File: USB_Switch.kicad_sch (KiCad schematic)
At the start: 1 part

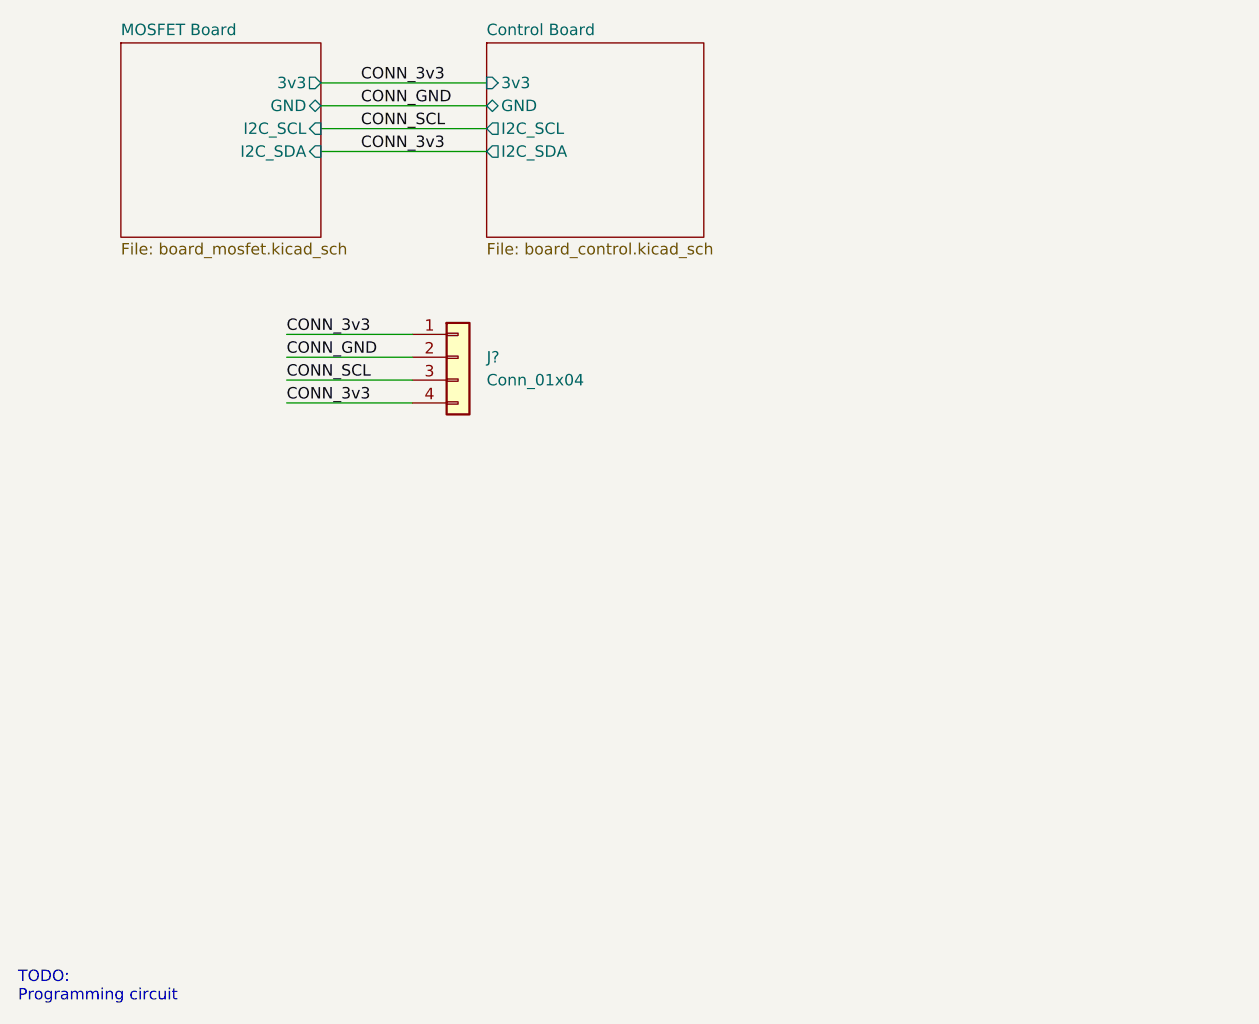
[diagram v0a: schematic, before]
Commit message: Fixed file name, started board layout
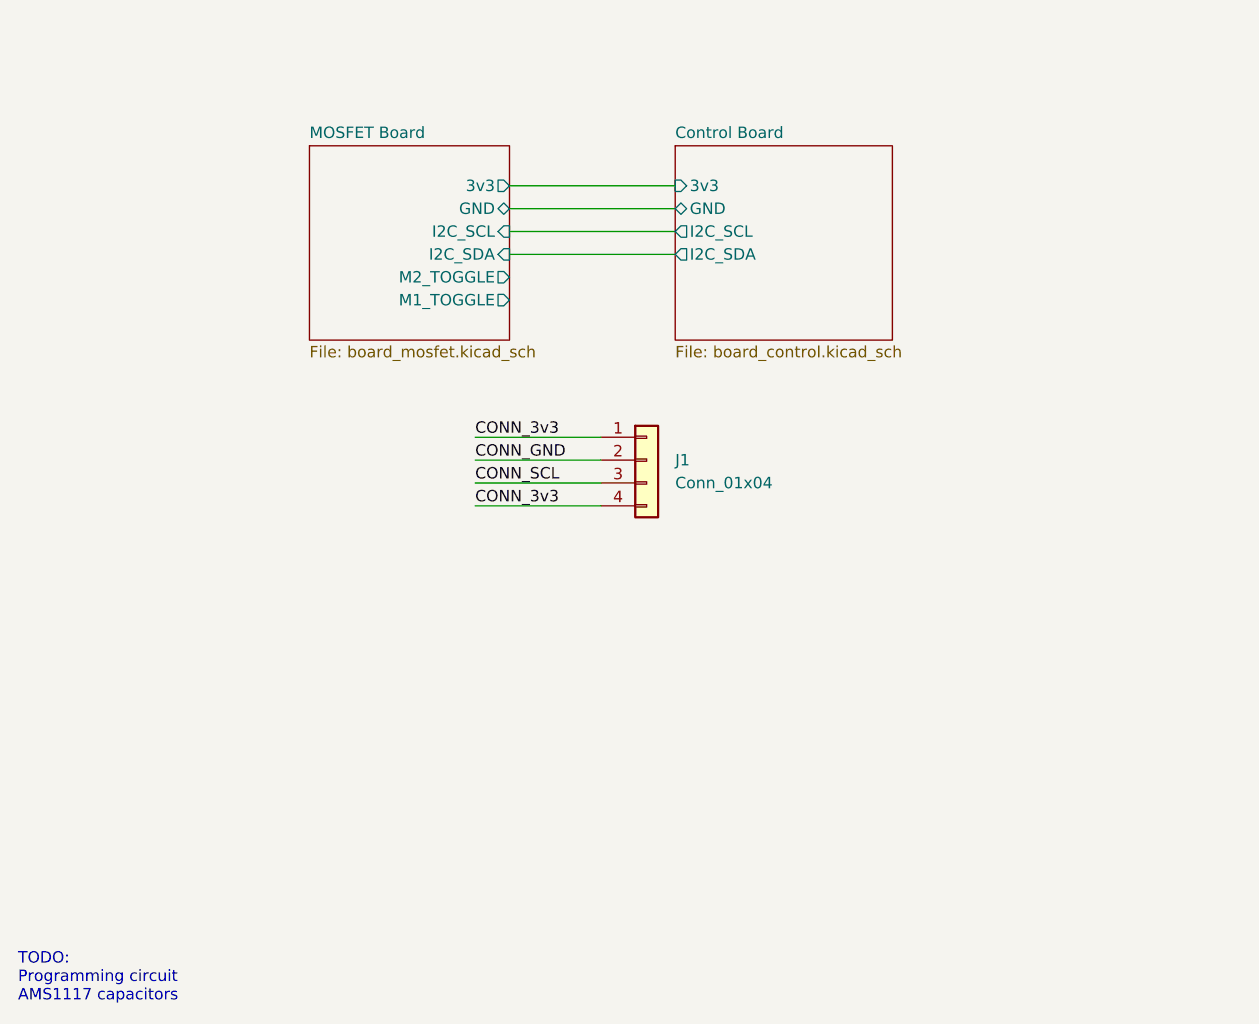
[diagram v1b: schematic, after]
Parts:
- gave numbers to parts that had none: 1
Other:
- sheet MOSFET Board ports: added M1_TOGGLE, M2_TOGGLE; removed none
- note added: "TODO: Programming circuit AMS1117 capacitors"
- note removed: "TODO: Programming circuit"
- moved on the sheet: J1

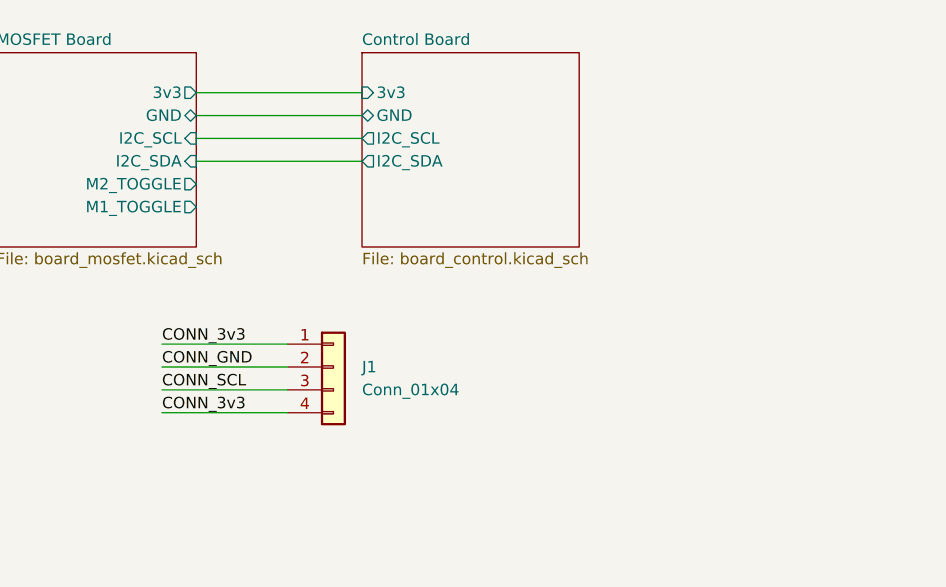
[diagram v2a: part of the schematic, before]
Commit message: Updated board connections. Added supplier info for all parts
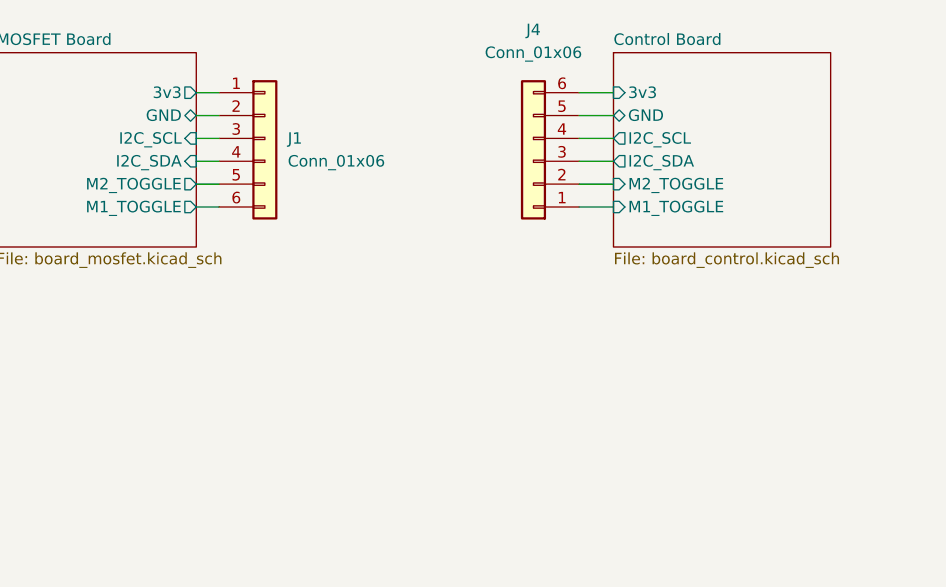
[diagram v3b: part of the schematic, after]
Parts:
- removed J1: Conn_01x04, symbol Connector_Generic:Conn_01x04
- added J1, J4: Conn_01x06, Connector_PinHeader_2.54mm:PinHeader_1x06_P2.54mm_Vertical, symbol Connector_Generic:Conn_01x06
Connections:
- net Control Board/3v3: now also J4.6 (Pin_6)
- net Control Board/GND: now also J4.5 (Pin_5)
- net Control Board/I2C_SCL: now also J4.4 (Pin_4)
- net Control Board/I2C_SDA: now also J4.3 (Pin_3)
- net MOSFET Board/M1_TOGGLE: now also J1.6 (Pin_6)
- net MOSFET Board/M2_TOGGLE: now also J1.5 (Pin_5)
- new net Control Board/M1_TOGGLE: J4.1 (Pin_1)
- new net Control Board/M2_TOGGLE: J4.2 (Pin_2)
- new net MOSFET Board/3v3: J1.1 (Pin_1)
- new net MOSFET Board/GND: J1.2 (Pin_2)
- new net MOSFET Board/I2C_SCL: J1.3 (Pin_3)
- new net MOSFET Board/I2C_SDA: J1.4 (Pin_4)
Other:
- sheet Control Board ports: added M1_TOGGLE, M2_TOGGLE; removed none

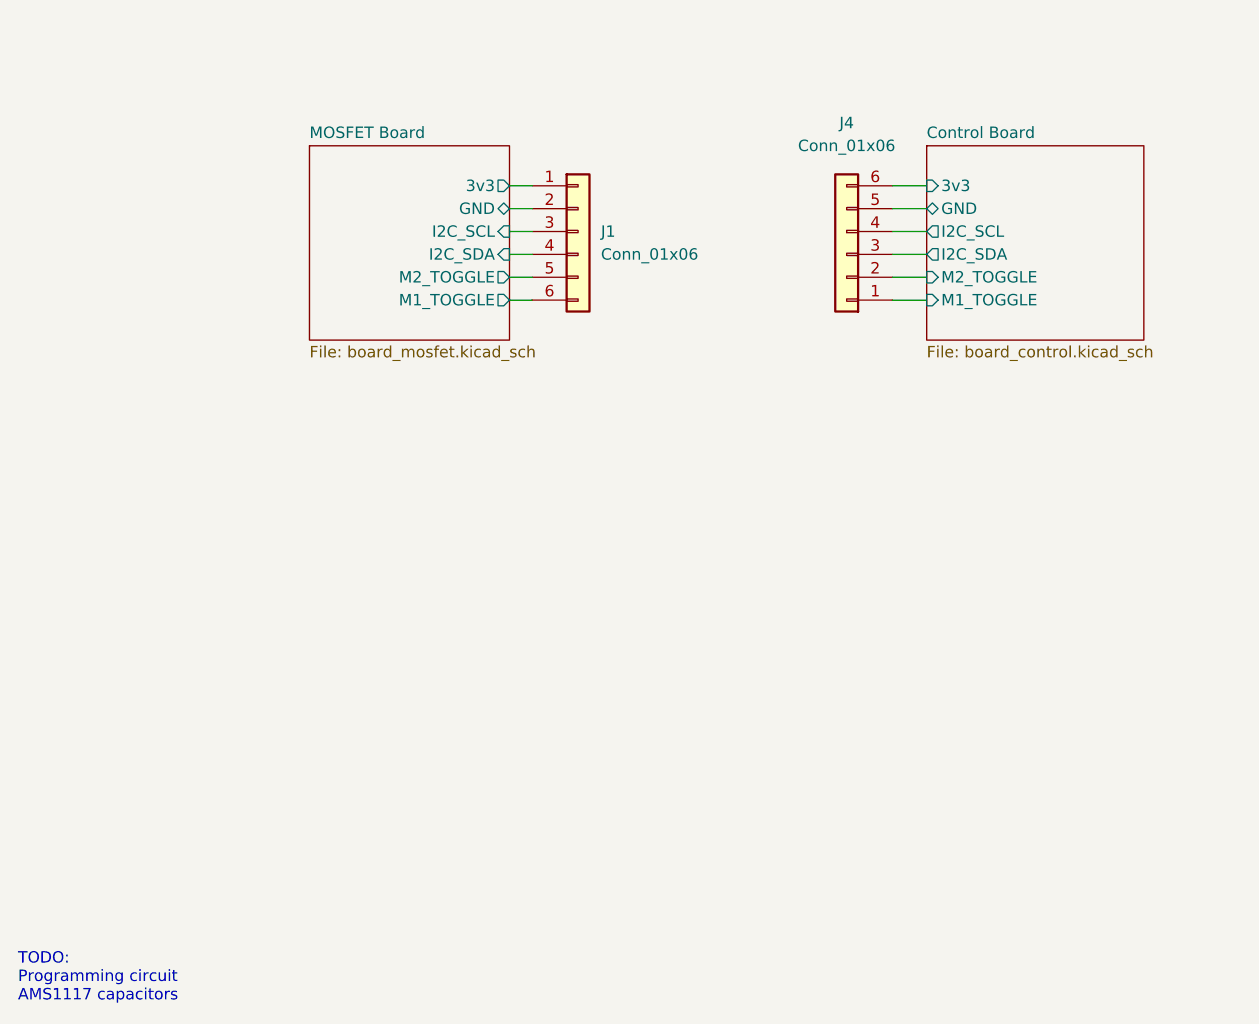
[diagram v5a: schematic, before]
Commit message: Added TX/RX to schematic. Updated PCB
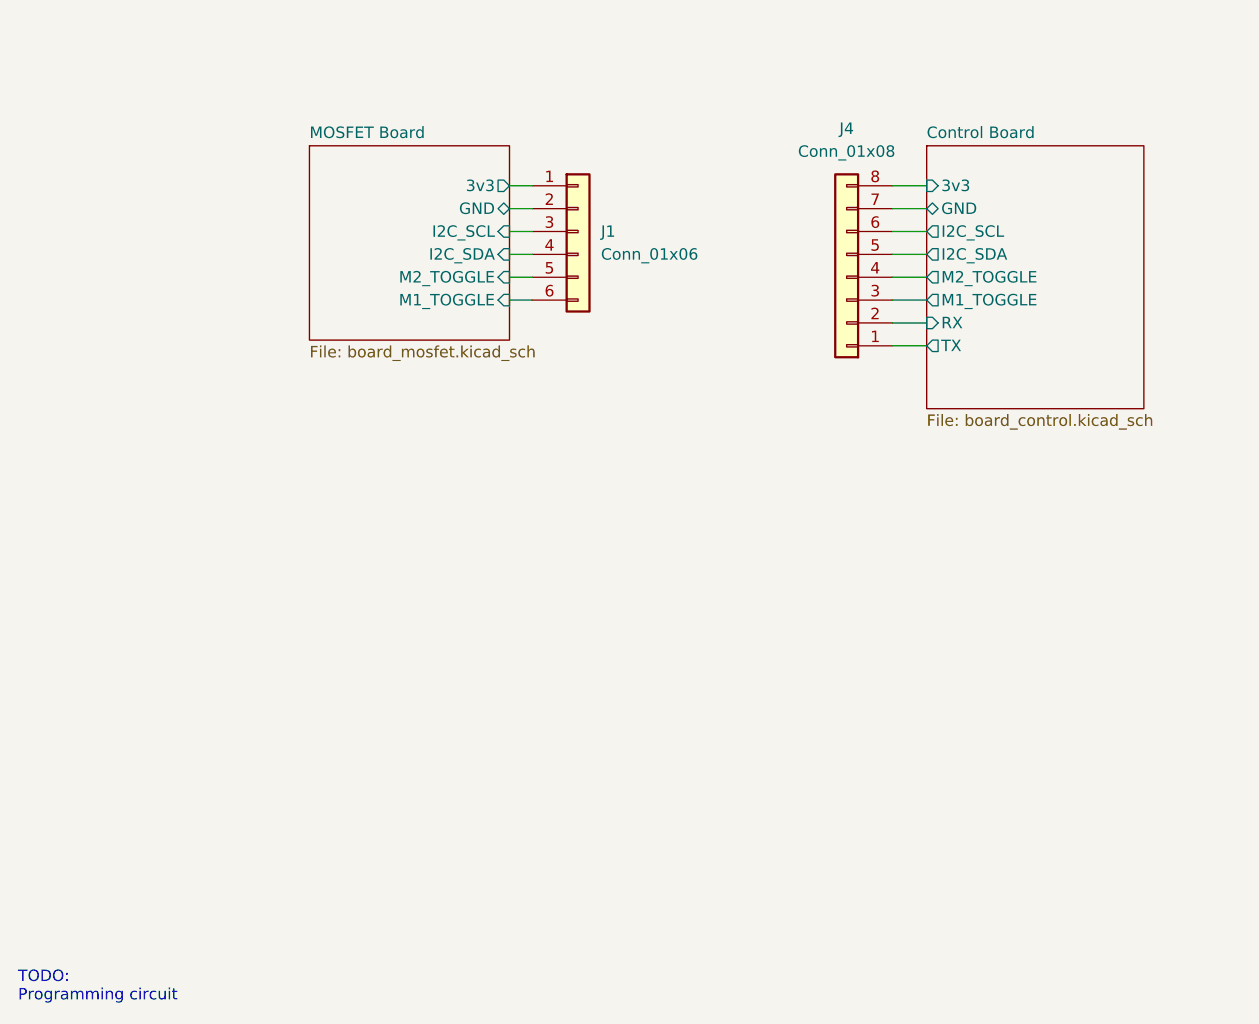
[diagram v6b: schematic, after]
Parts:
- removed J4: Conn_01x06, Connector_PinHeader_2.54mm:PinHeader_1x06_P2.54mm_Vertical, symbol Connector_Generic:Conn_01x06
- added J4: Conn_01x08, Connector_PinHeader_2.54mm:PinHeader_1x08_P2.54mm_Vertical, symbol Connector_Generic:Conn_01x08
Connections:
- net Control Board/3v3: now also J4.8 (Pin_8)
- net Control Board/GND: now also J4.7 (Pin_7)
- net Control Board/I2C_SCL: now also J4.6 (Pin_6)
- net Control Board/I2C_SDA: now also J4.5 (Pin_5)
- net Control Board/M1_TOGGLE: now also J4.3 (Pin_3)
- net Control Board/M2_TOGGLE: now also J4.4 (Pin_4)
- new net Control Board/RX: J4.2 (Pin_2)
- new net Control Board/TX: J4.1 (Pin_1)
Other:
- sheet Control Board ports: added RX, TX; removed none
- note added: "TODO: Programming circuit"
- note removed: "TODO: Programming circuit AMS1117 capacitors"
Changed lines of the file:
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@@
+    (stroke (width 0) (type default) (color 0 0 0 0))
+  )
+  (wire (pts (xy 137.795 64.135) (xy 141.605 64.135))
     (stroke (width 0) (type default) (color 0 0 0 0))
   )
@@
     (stroke (width 0) (type default) (color 0 0 0 0))
   )
+  (wire (pts (xy 137.795 66.675) (xy 141.605 66.675))
+    (stroke (width 0) (type default) (color 0 0 0 0))
+  )
   (wire (pts (xy 137.795 56.515) (xy 141.605 56.515))
     (stroke (width 0) (type default) (color 0 0 0 0))
   )
-  (text "TODO:\nProgramming circuit\nAMS1117 capacitors" (at 40.64 139.7 0)
+  (text "TODO:\nProgramming circuit" (at 40.64 139.7 0)
     (effects (font (size 1.27 1.27)) (justify left bottom))
   )
-  (symbol (lib_id "Connector_Generic:Conn_01x06") (at 132.715 56.515 180) (unit 1)
+  (symbol (lib_id "Connector_Generic:Conn_01x08") (at 132.715 59.055 180) (unit 1)
     (in_bom yes) (on_board yes) (fields_autoplaced)
-    (property "Reference" "J4" (id 0) (at 132.715 41.91 0))
-    (property "Value" "Conn_01x06" (id 1) (at 132.715 44.45 0))
-    (property "Footprint" "Connector_PinHeader_2.54mm:PinHeader_1x06_P2.54mm_Vertical" (id 2) (at 132.715 56.515 0)
-      (effects (font (size 1.27 1.27)) hide)
-    )
-    (property "Datasheet" "~" (id 3) (at 132.715 56.515 0)
-      (effects (font (size 1.27 1.27)) hide)
-    )
-    (property "LCSC Part Number" "" (id 4) (at 132.715 56.515 0)
-      (effects (font (size 1.27 1.27)) hide)
-    )
-    (property "Manufacturer" "" (id 5) (at 132.715 56.515 0)
-      (effects (font (size 1.27 1.27)) hide)
-    )
-    (property "Manufacturer Part Number" "" (id 6) (at 132.715 56.515 0)
+    (property "Reference" "J4" (id 0) (at 132.715 42.545 0))
+    (property "Value" "Conn_01x08" (id 1) (at 132.715 45.085 0))
+    (property "Footprint" "Connector_PinHeader_2.54mm:PinHeader_1x08_P2.54mm_Vertical" (id 2) (at 132.715 59.055 0)
+      (effects (font (size 1.27 1.27)) hide)
+    )
+    (property "Datasheet" "~" (id 3) (at 132.715 59.055 0)
       (effects (font (size 1.27 1.27)) hide)
     )
@@
     (pin "5")
     (pin "6")
+    (pin "7")
+    (pin "8")
   )
   (symbol (lib_id "Connector_Generic:Conn_01x06") (at 102.87 53.975 0) (unit 1)
@@
     (pin "6")
   )
-  (sheet (at 141.605 44.45) (size 24.13 21.59) (fields_autoplaced)
+  (sheet (at 141.605 44.45) (size 24.13 29.21) (fields_autoplaced)
     (stroke (width 0.1524) (type solid) (color 0 0 0 0))
     (fill (color 0 0 0 0.0000))
@@
       (effects (font (size 1.27 1.27)) (justify left bottom))
     )
-    (property "Sheet file" "board_control.kicad_sch" (id 1) (at 141.605 66.6246 0)
+    (property "Sheet file" "board_control.kicad_sch" (id 1) (at 141.605 74.2446 0)
       (effects (font (size 1.27 1.27)) (justify left top))
     )
@@
       (effects (font (size 1.27 1.27)) (justify left))
     )
-    (pin "M2_TOGGLE" input (at 141.605 59.055 180)
-      (effects (font (size 1.27 1.27)) (justify left))
-    )
-    (pin "M1_TOGGLE" input (at 141.605 61.595 180)
+    (pin "M2_TOGGLE" output (at 141.605 59.055 180)
+      (effects (font (size 1.27 1.27)) (justify left))
+    )
+    (pin "M1_TOGGLE" output (at 141.605 61.595 180)
+      (effects (font (size 1.27 1.27)) (justify left))
+    )
+    (pin "TX" output (at 141.605 66.675 180)
+      (effects (font (size 1.27 1.27)) (justify left))
+    )
+    (pin "RX" input (at 141.605 64.135 180)
       (effects (font (size 1.27 1.27)) (justify left))
     )
@@
       (effects (font (size 1.27 1.27)) (justify right))
     )
-    (pin "M2_TOGGLE" output (at 95.25 59.055 0)
-      (effects (font (size 1.27 1.27)) (justify right))
-    )
-    (pin "M1_TOGGLE" output (at 95.25 61.595 0)
+    (pin "M2_TOGGLE" input (at 95.25 59.055 0)
+      (effects (font (size 1.27 1.27)) (justify right))
+    )
+    (pin "M1_TOGGLE" input (at 95.25 61.595 0)
       (effects (font (size 1.27 1.27)) (justify right))
     )
@@
       (reference "#PWR011") (unit 1) (value "GND") (footprint "")
     )
-    (path "/24a3ebde-e6d3-496d-9465-03105f52e4c1/db1356a0-03ad-4791-94db-e27389fa297b"
-      (reference "#PWR012") (unit 1) (value "GND") (footprint "")
-    )
     (path "/24a3ebde-e6d3-496d-9465-03105f52e4c1/9b7a36b0-b698-4371-b578-de0a598cea00"
       (reference "#PWR013") (unit 1) (value "GND") (footprint "")
@@
       (reference "#PWR0101") (unit 1) (value "GND") (footprint "")
     )
+    (path "/24a3ebde-e6d3-496d-9465-03105f52e4c1/d1c38565-6dd1-4355-87c6-fd902a3e6b30"
+      (reference "#PWR0102") (unit 1) (value "GND") (footprint "")
+    )
     (path "/4fe24247-d6eb-4bd9-871f-ba2a853fda03/b1347e55-543f-45da-a2d4-4eeca306373d"
       (reference "C1") (unit 1) (value "100nF") (footprint "Capacitor_SMD:C_0603_1608Metric")
@@
       (reference "J3") (unit 1) (value "USB_OUT") (footprint "Library:904-131A2032S10100")
     )
-    (path "/3f2aa8b8-a32b-4aac-b22a-f5d706f9a77a"
-      (reference "J4") (unit 1) (value "Conn_01x06") (footprint "Connector_PinHeader_2.54mm:PinHeader_1x06_P2.54mm_Vertical")
+    (path "/6e72a175-2d14-4216-b462-9055574066fa"
+      (reference "J4") (unit 1) (value "Conn_01x08") (footprint "Connector_PinHeader_2.54mm:PinHeader_1x08_P2.54mm_Vertical")
     )
     (path "/4fe24247-d6eb-4bd9-871f-ba2a853fda03/7b71fcd5-794c-4ec8-8a59-c0463325c723"
